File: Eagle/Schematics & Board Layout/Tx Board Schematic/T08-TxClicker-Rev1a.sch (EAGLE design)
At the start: 98 parts, among them U1 CC430F513X---RGZ48, X1-DNI SMA-SMD, Y1 26MHz

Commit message: O.O
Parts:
- added X1-DNI1: SMA-SMD, con-coax:SMA-SMD
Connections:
- new net TEST50: X1-DNI1.1
- net GND: now also X1-DNI1.2
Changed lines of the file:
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@@
 <part name="TP25" library="SparkFun-Passives" deviceset="TEST-POINT" device="3"/>
 <part name="TP26" library="SparkFun-Passives" deviceset="TEST-POINT" device="3"/>
+<part name="X1-DNI1" library="con-coax" deviceset="SMA-SMD" device=""/>
+<part name="SUPPLY15" library="supply2" deviceset="GND" device=""/>
 </parts>
 <sheets>
@@
 <attribute name="NAME" x="86.36" y="190.5" size="1.778" layer="95" font="vector" rot="R180"/>
 </instance>
+<instance part="X1-DNI1" gate="G$1" x="162.56" y="22.86" smashed="yes" rot="R270">
+<attribute name="VALUE" x="157.48" y="25.4" size="1.778" layer="96"/>
+<attribute name="NAME" x="165.1" y="21.082" size="1.778" layer="95"/>
+</instance>
+<instance part="SUPPLY15" gate="GND" x="160.02" y="17.78" smashed="yes">
+<attribute name="VALUE" x="153.035" y="17.145" size="1.778" layer="96"/>
+</instance>
 </instances>
 <busses>
@@
 <pinref part="SUPPLY18" gate="GND" pin="GND"/>
 </segment>
+<segment>
+<pinref part="X1-DNI1" gate="G$1" pin="2"/>
+<pinref part="SUPPLY15" gate="GND" pin="GND"/>
+</segment>
 </net>
 <net name="VCC" class="0">
@@
 </segment>
 </net>
+<net name="TEST50" class="0">
+<segment>
+<pinref part="X1-DNI1" gate="G$1" pin="1"/>
+<wire x1="162.56" y1="20.32" x2="162.56" y2="17.78" width="0.1524" layer="91"/>
+</segment>
+</net>

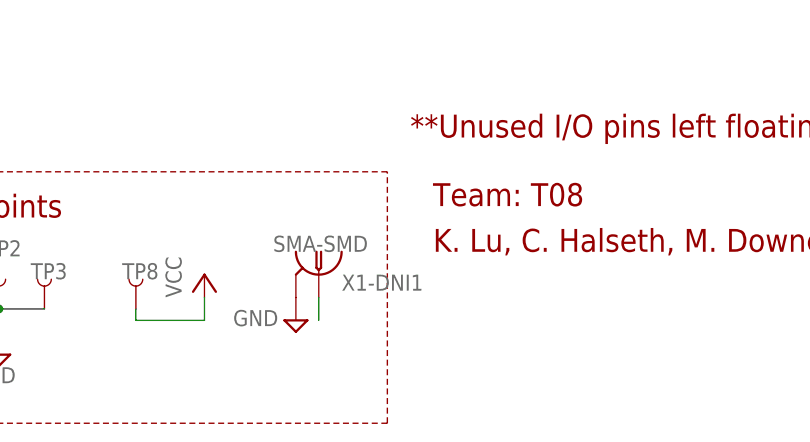
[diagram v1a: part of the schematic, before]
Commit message: Updated silkscreen, added board preview
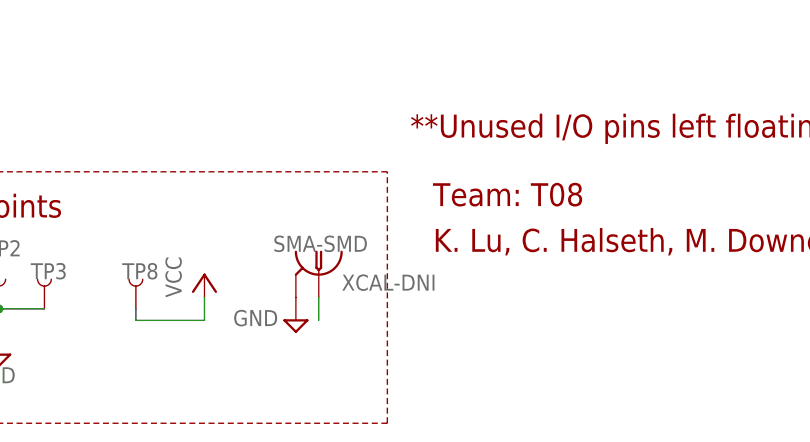
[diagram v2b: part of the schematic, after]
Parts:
- renumbered X1-DNI1 to XCAL-DNI
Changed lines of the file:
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@@
 <?xml version="1.0" encoding="utf-8"?>
 <!DOCTYPE eagle SYSTEM "eagle.dtd">
-<eagle version="7.1.0">
+<eagle version="6.4">
 <drawing>
 <settings>
@@
 <part name="TP25" library="SparkFun-Passives" deviceset="TEST-POINT" device="3"/>
 <part name="TP26" library="SparkFun-Passives" deviceset="TEST-POINT" device="3"/>
-<part name="X1-DNI1" library="con-coax" deviceset="SMA-SMD" device=""/>
+<part name="XCAL-DNI" library="con-coax" deviceset="SMA-SMD" device=""/>
 <part name="SUPPLY15" library="supply2" deviceset="GND" device=""/>
 </parts>
@@
 <attribute name="NAME" x="86.36" y="190.5" size="1.778" layer="95" font="vector" rot="R180"/>
 </instance>
-<instance part="X1-DNI1" gate="G$1" x="162.56" y="22.86" smashed="yes" rot="R270">
+<instance part="XCAL-DNI" gate="G$1" x="162.56" y="22.86" smashed="yes" rot="R270">
 <attribute name="VALUE" x="157.48" y="25.4" size="1.778" layer="96"/>
 <attribute name="NAME" x="165.1" y="21.082" size="1.778" layer="95"/>
@@
 </segment>
 <segment>
-<pinref part="X1-DNI1" gate="G$1" pin="2"/>
+<pinref part="XCAL-DNI" gate="G$1" pin="2"/>
 <pinref part="SUPPLY15" gate="GND" pin="GND"/>
 </segment>
@@
 <net name="TEST50" class="0">
 <segment>
-<pinref part="X1-DNI1" gate="G$1" pin="1"/>
+<pinref part="XCAL-DNI" gate="G$1" pin="1"/>
 <wire x1="162.56" y1="20.32" x2="162.56" y2="17.78" width="0.1524" layer="91"/>
 </segment>
